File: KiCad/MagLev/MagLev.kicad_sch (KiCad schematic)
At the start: 64 parts, among them J1 FC681465S, Q11 MMBT3904, Q12 AOD442G, Q13 AOD442G, Q18 ZX5T1951GTA, Q5 ZX5T1951GTA, U10 X, U11 Y, U12 Z, U13 MCP1402, U14 MCP1402, U3 L78L05_SO8, U4 TL431A, U5 LM393, X1 L_Ferrite, X2 L_Ferrite, Y1 L_Ferrite, Y2 L_Ferrite, Y5 L_Ferrite, Y6 L_Ferrite, Y8 L_Ferrite, Y9 L_Ferrite

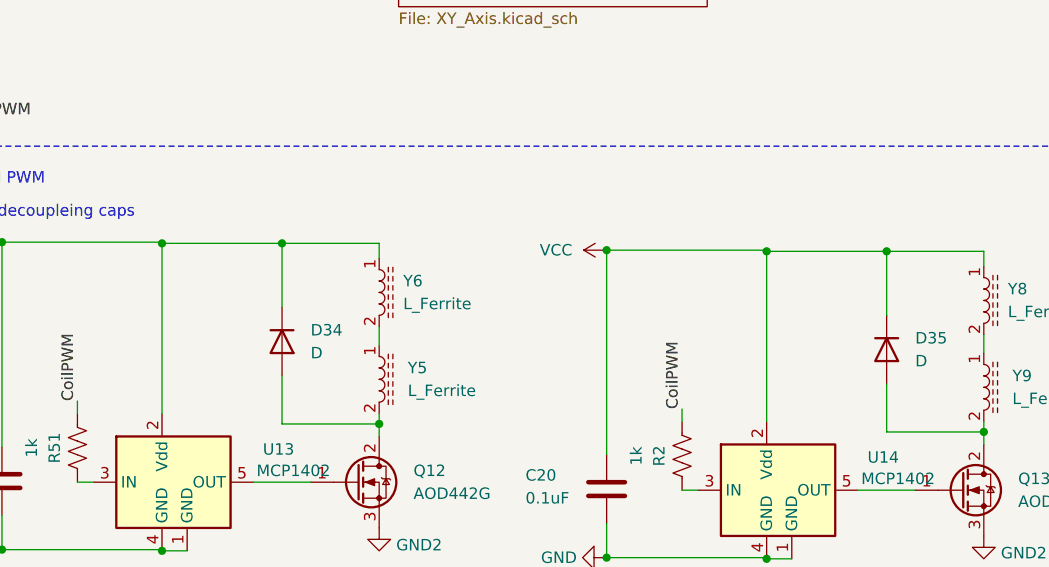
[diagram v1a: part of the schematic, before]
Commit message: Add decoupling caps to PWM switching Fets.
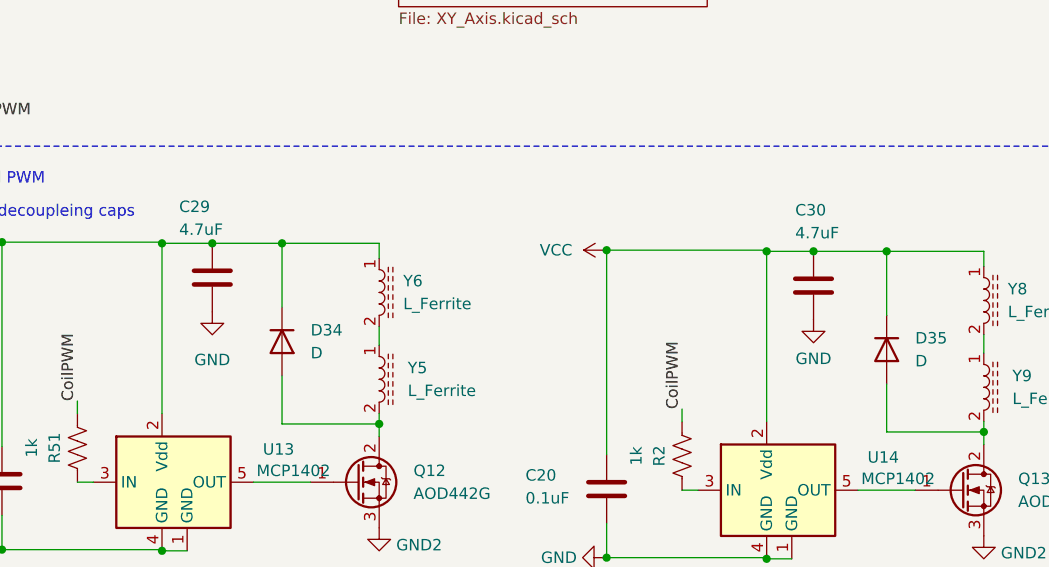
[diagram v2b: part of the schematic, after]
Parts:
- added C29, C30: 4.7uF, Capacitor_SMD:C_0805_2012Metric_Pad1.18x1.45mm_HandSolder, symbol Device:C
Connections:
- net GND: now also C29.2, C30.2
- net VCC: now also C29.1, C30.1
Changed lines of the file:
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@@
   (junction (at 53.975 179.832) (diameter 0) (color 0 0 0 0)
   )
+  (junction (at 183.769 111.633) (diameter 0) (color 0 0 0 0)
+  )
   (junction (at 74.168 145.415) (diameter 0) (color 0 0 0 0)
   )
+  (junction (at 250.571 112.522) (diameter 0) (color 0 0 0 0)
+  )
   (junction (at 51.816 144.145) (diameter 0) (color 0 0 0 0)
   )
@@
     (stroke (width 0) (type default))
   )
+  (wire (pts (xy 250.571 112.522) (xy 245.364 112.522))
+    (stroke (width 0) (type default))
+  )
   (wire (pts (xy 114.3 128.143) (xy 128.27 128.143))
     (stroke (width 0) (type default))
@@
     (stroke (width 0) (type default))
   )
-  (wire (pts (xy 191.516 111.633) (xy 178.181 111.633))
+  (wire (pts (xy 191.516 111.633) (xy 183.769 111.633))
     (stroke (width 0) (type default))
   )
@@
     (stroke (width 0) (type default))
   )
-  (wire (pts (xy 258.699 112.522) (xy 245.364 112.522))
+  (wire (pts (xy 258.699 112.522) (xy 250.571 112.522))
     (stroke (width 0) (type default))
   )
@@
     (stroke (width 0) (type default))
   )
+  (wire (pts (xy 183.769 111.633) (xy 178.181 111.633))
+    (stroke (width 0) (type default))
+  )
   (wire (pts (xy 128.27 131.953) (xy 128.27 128.143))
     (stroke (width 0) (type default))
@@
     )
   )
-  (netclass_flag "" (length 2.54) (shape round) (at 184.15 111.633 0) (fields_autoplaced)
+  (netclass_flag "" (length 2.54) (shape round) (at 194.564 111.633 0) (fields_autoplaced)
     (effects (font (size 1.27 1.27)) (justify left bottom))
-    (property "Netclass" "HighCurrent" (at 184.8485 109.093 0)
+    (property "Netclass" "HighCurrent" (at 195.2625 109.093 0)
       (effects (font (size 1.27 1.27) italic) (justify left))
     )
@@
     )
   )
+  (symbol (lib_id "power:GND") (at 250.571 120.142 0) (unit 1)
+    (in_bom yes) (on_board yes) (dnp no) (fields_autoplaced)
+    (property "Reference" "#PWR059" (at 250.571 126.492 0)
+      (effects (font (size 1.27 1.27)) hide)
+    )
+    (property "Value" "GND" (at 250.571 124.46 0)
+      (effects (font (size 1.27 1.27)))
+    )
+    (property "Footprint" "" (at 250.571 120.142 0)
+      (effects (font (size 1.27 1.27)) hide)
+    )
+    (property "Datasheet" "" (at 250.571 120.142 0)
+      (effects (font (size 1.27 1.27)) hide)
+    )
+    (pin "1")
+    (instances
+      (project "MagLev"
+        (path "/5eab7e8b-54e1-47d0-9dc3-1e7c3fa2f560"
+          (reference "#PWR059") (unit 1)
+        )
+      )
+    )
+  )
   (symbol (lib_id "power:GND") (at 160.274 145.669 270) (unit 1)
     (in_bom yes) (on_board yes) (dnp no) (fields_autoplaced)
@@
     )
   )
+  (symbol (lib_id "power:GND") (at 183.769 119.253 0) (unit 1)
+    (in_bom yes) (on_board yes) (dnp no) (fields_autoplaced)
+    (property "Reference" "#PWR057" (at 183.769 125.603 0)
+      (effects (font (size 1.27 1.27)) hide)
+    )
+    (property "Value" "GND" (at 183.769 124.587 0)
+      (effects (font (size 1.27 1.27)))
+    )
+    (property "Footprint" "" (at 183.769 119.253 0)
+      (effects (font (size 1.27 1.27)) hide)
+    )
+    (property "Datasheet" "" (at 183.769 119.253 0)
+      (effects (font (size 1.27 1.27)) hide)
+    )
+    (pin "1")
+    (instances
+      (project "MagLev"
+        (path "/5eab7e8b-54e1-47d0-9dc3-1e7c3fa2f560"
+          (reference "#PWR057") (unit 1)
+        )
+      )
+    )
+  )
   (symbol (lib_id "Mechanical:MountingHole_Pad") (at 162.052 159.766 270) (unit 1)
     (in_bom yes) (on_board yes) (dnp no) (fields_autoplaced)
@@
     )
   )
+  (symbol (lib_id "Device:C") (at 183.769 115.443 0) (unit 1)
+    (in_bom yes) (on_board yes) (dnp no)
+    (property "Reference" "C29" (at 180.086 107.569 0)
+      (effects (font (size 1.27 1.27)) (justify left))
+    )
+    (property "Value" "4.7uF" (at 180.086 110.109 0)
+      (effects (font (size 1.27 1.27)) (justify left))
+    )
+    (property "Footprint" "Capacitor_SMD:C_0805_2012Metric_Pad1.18x1.45mm_HandSolder" (at 184.7342 119.253 0)
+      (effects (font (size 1.27 1.27)) hide)
+    )
+    (property "Datasheet" "~" (at 183.769 115.443 0)
+      (effects (font (size 1.27 1.27)) hide)
+    )
+    (pin "1")
+    (pin "2")
+    (instances
+      (project "MagLev"
+        (path "/5eab7e8b-54e1-47d0-9dc3-1e7c3fa2f560"
+          (reference "C29") (unit 1)
+        )
+        (path "/5eab7e8b-54e1-47d0-9dc3-1e7c3fa2f560/1b1a7f40-4880-4dc8-87d1-1ed1d4fb8d1e"
+          (reference "C8") (unit 1)
+        )
+        (path "/5eab7e8b-54e1-47d0-9dc3-1e7c3fa2f560/7df46fb0-abf8-474a-ba30-7ff9455482b6"
+          (reference "C1") (unit 1)
+        )
+      )
+    )
+  )
   (symbol (lib_id "Device:L_Ferrite") (at 254 73.914 180) (unit 1)
     (in_bom yes) (on_board yes) (dnp no) (fields_autoplaced)
@@
         )
       )
+    )
+  )
+  (symbol (lib_id "Device:C") (at 250.571 116.332 0) (unit 1)
+    (in_bom yes) (on_board yes) (dnp no)
+    (property "Reference" "C30" (at 248.539 107.95 0)
+      (effects (font (size 1.27 1.27)) (justify left))
+    )
+    (property "Value" "4.7uF" (at 248.539 110.49 0)
+      (effects (font (size 1.27 1.27)) (justify left))
+    )
+    (property "Footprint" "Capacitor_SMD:C_0805_2012Metric_Pad1.18x1.45mm_HandSolder" (at 251.5362 120.142 0)
+      (effects (font (size 1.27 1.27)) hide)
+    )
+    (property "Datasheet" "~" (at 250.571 116.332 0)
+      (effects (font (size 1.27 1.27)) hide)
+    )
+    (pin "1")
+    (pin "2")
+    (instances
+      (project "MagLev"
+        (path "/5eab7e8b-54e1-47d0-9dc3-1e7c3fa2f560"
+          (reference "C30") (unit 1)
+        )
+        (path "/5eab7e8b-54e1-47d0-9dc3-1e7c3fa2f560/1b1a7f40-4880-4dc8-87d1-1ed1d4fb8d1e"
+          (reference "C8") (unit 1)
+        )
+        (path "/5eab7e8b-54e1-47d0-9dc3-1e7c3fa2f560/7df46fb0-abf8-474a-ba30-7ff9455482b6"
+          (reference "C1") (unit 1)
+        )
+      )

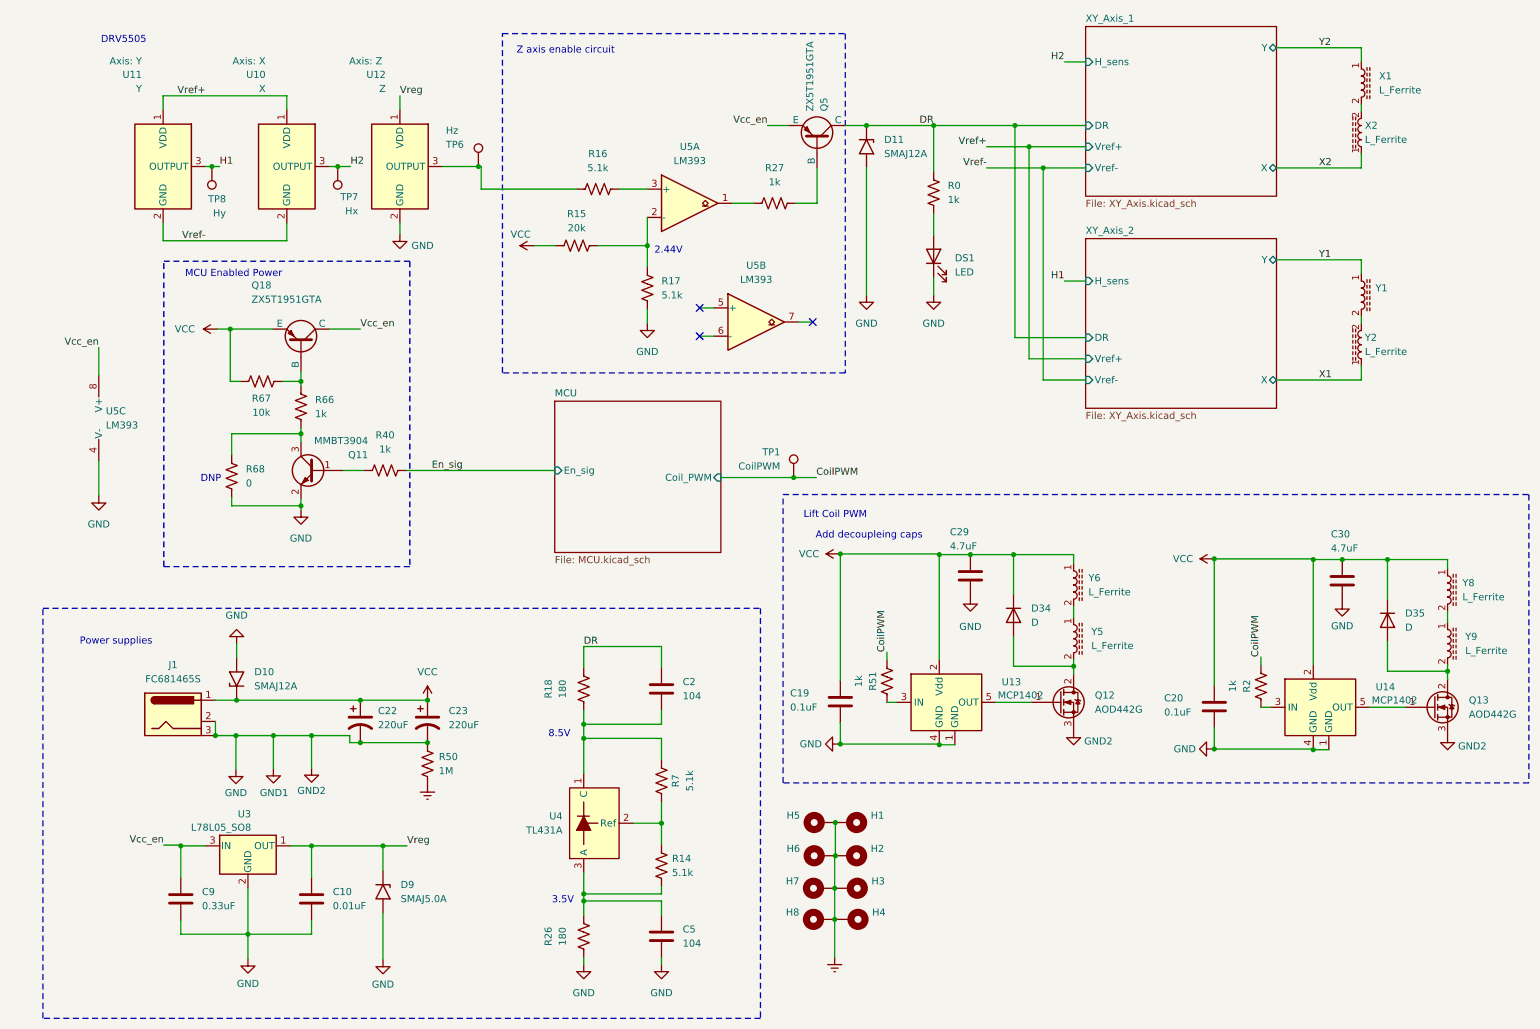
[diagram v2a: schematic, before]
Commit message: Review all footprints.
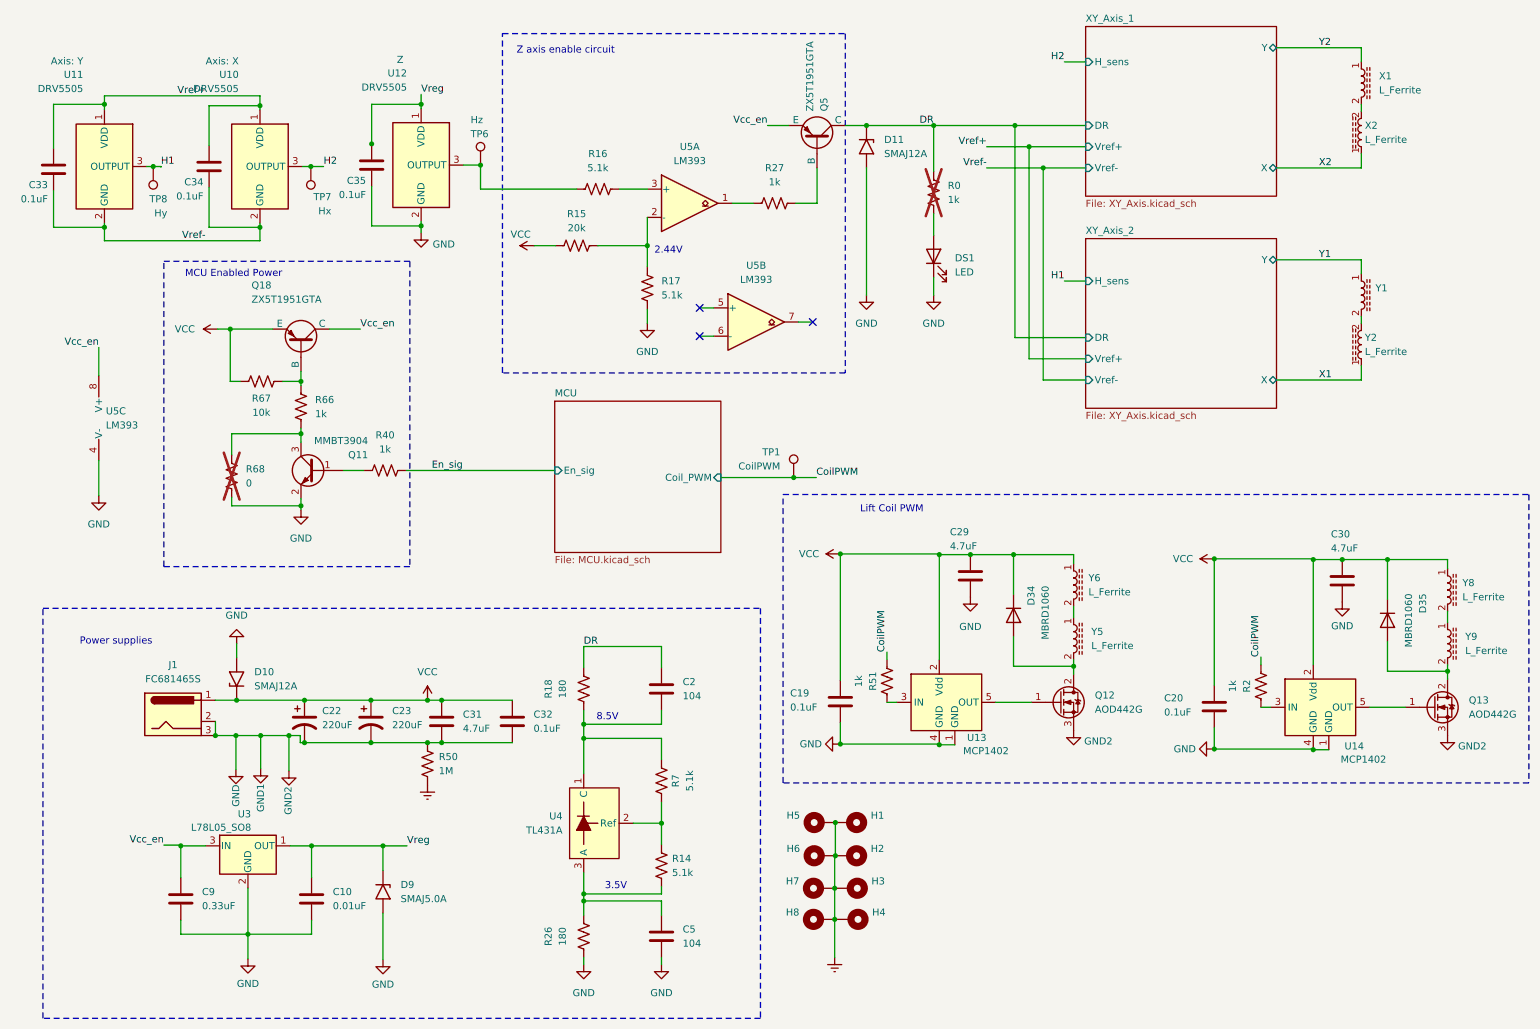
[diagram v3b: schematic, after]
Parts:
- added C31: 4.7uF, Capacitor_SMD:C_0805_2012Metric_Pad1.18x1.45mm_HandSolder, symbol Device:C
- added C32, C33, C34, C35: 0.1uF, Capacitor_SMD:C_0805_2012Metric_Pad1.18x1.45mm_HandSolder, symbol Device:C
- D34, D35: value D -> MBRD1060
- R0, R68: now not fitted
- U10: value X -> DRV5505
- U11: value Y -> DRV5505
- U12: value Z -> DRV5505
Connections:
- net GND: now also C31.2, C32.2, C35.2
- net VCC: now also C31.1, C32.1
- net Vref+: now also C33.1, C34.1
- net Vref-: now also C33.2, C34.2
- net Vreg: now also C35.1
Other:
- note removed: "Add decoupleing caps"
- note removed: "DNP"
- note removed: "DRV5505"
- moved on the sheet: C22, C23, TP7, TP8, U10, U11, U12

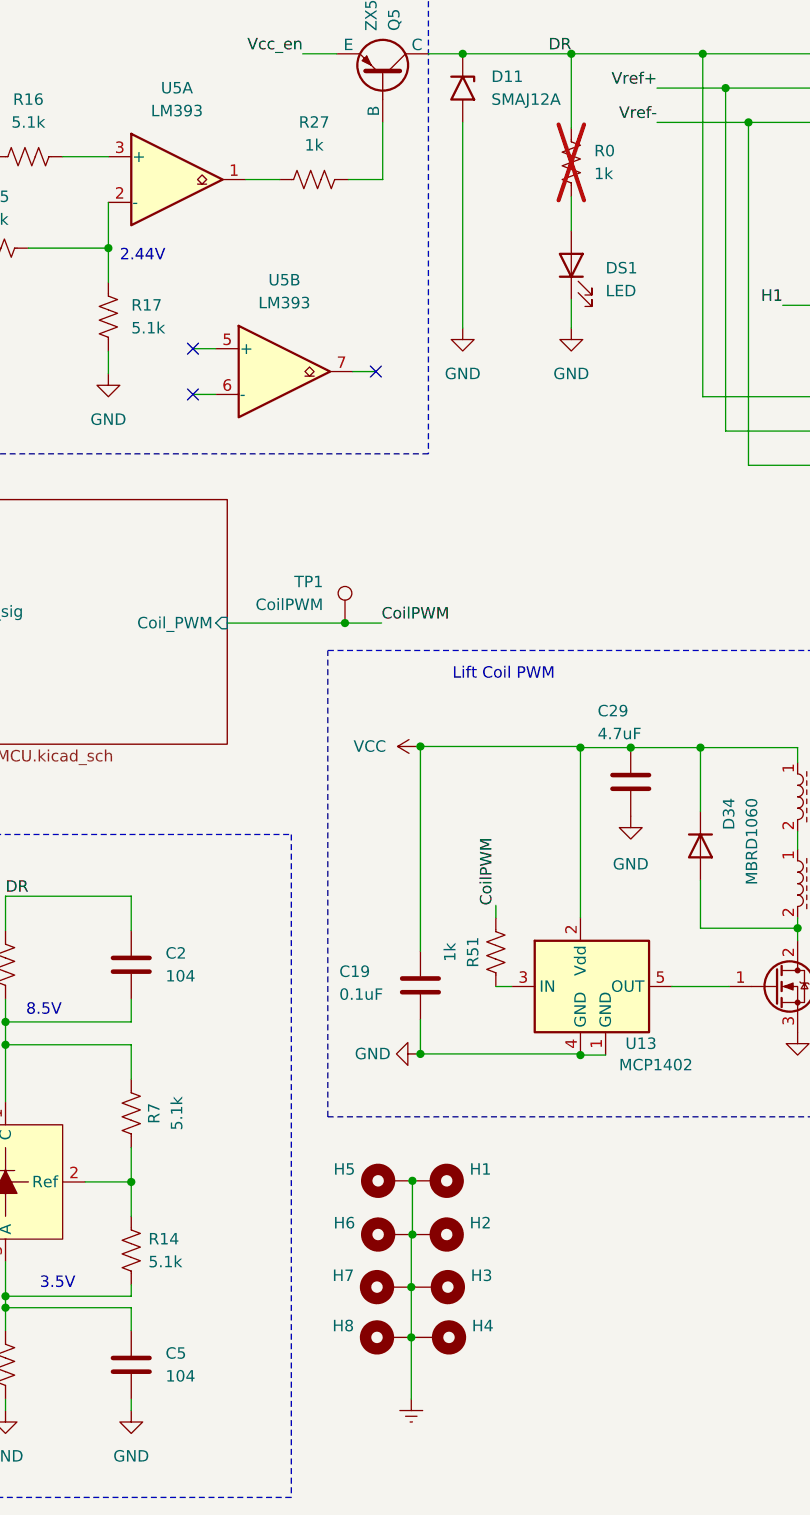
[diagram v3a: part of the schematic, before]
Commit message: Set LED bias resistors. Move MCU status LEDs to PWM pins.
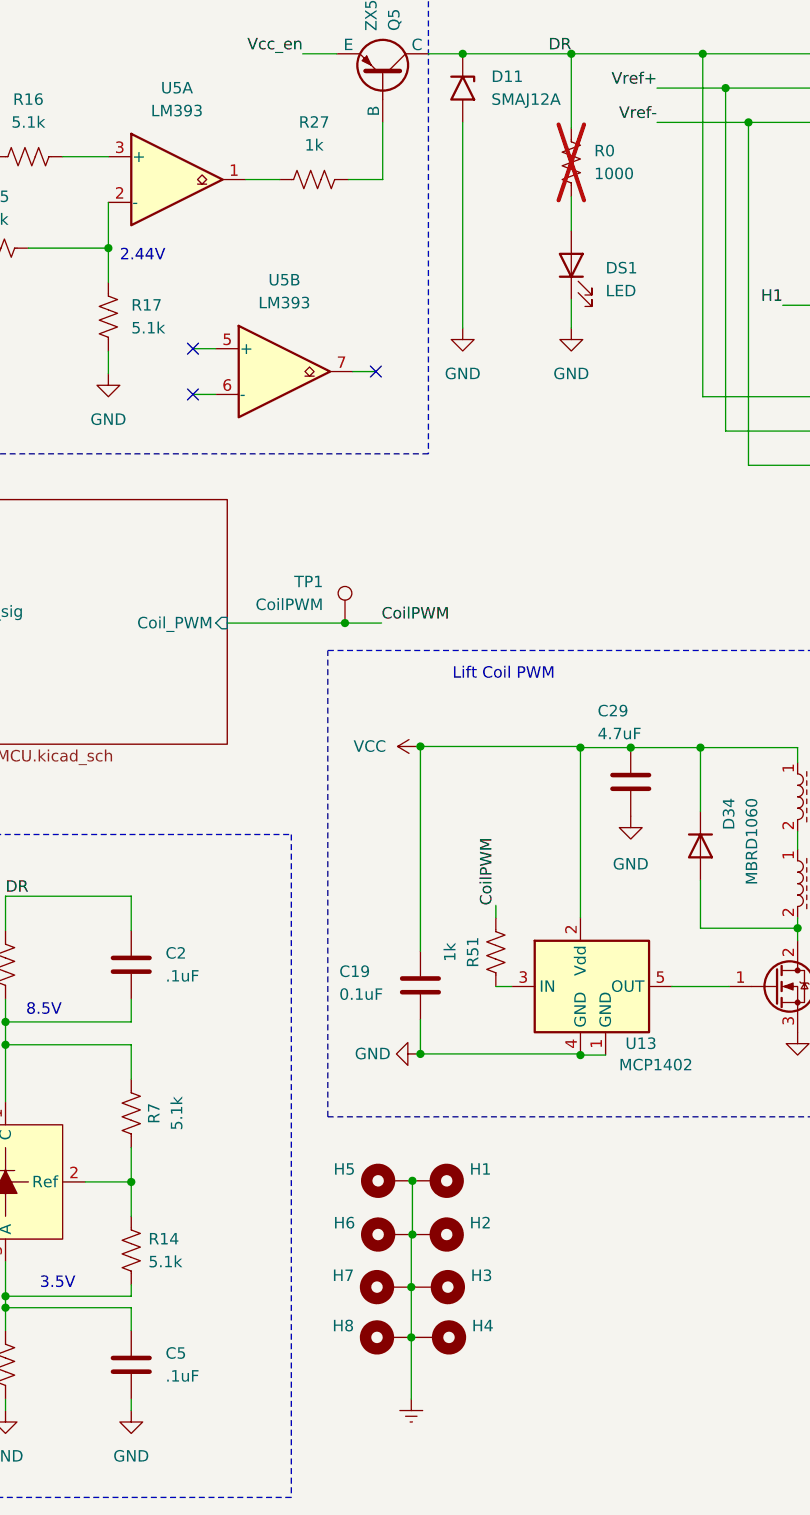
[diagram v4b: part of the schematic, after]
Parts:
- C2, C5: value 104 -> .1uF
- DS1: Part (none) -> SML-LXT0805IW-TR
- R0: value 1k -> 1000
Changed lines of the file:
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@@
       (effects (font (size 1.27 1.27)) (justify left))
     )
-    (property "Value" "104" (at 132.08 181.483 0)
+    (property "Value" ".1uF" (at 132.08 181.483 0)
       (effects (font (size 1.27 1.27)) (justify left))
     )
@@
     )
     (property "Datasheet" "~" (at 177.165 58.039 0)
+      (effects (font (size 1.27 1.27)) hide)
+    )
+    (property "Part" "SML-LXT0805IW-TR" (at 177.165 58.039 90)
       (effects (font (size 1.27 1.27)) hide)
     )
@@
       (effects (font (size 1.27 1.27)) (justify left))
     )
-    (property "Value" "104" (at 132.08 137.033 0)
+    (property "Value" ".1uF" (at 132.08 137.033 0)
       (effects (font (size 1.27 1.27)) (justify left))
     )
@@
       (effects (font (size 1.27 1.27)) (justify left))
     )
-    (property "Value" "1k" (at 179.705 47.879 0)
-      (effects (font (size 1.27 1.27)) (justify left))
-    )
+    (property "Value" "1000" (at 179.705 47.879 0)
+      (effects (font (size 1.27 1.27)) (justify left))
+    )
